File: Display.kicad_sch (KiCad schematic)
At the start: 2 parts

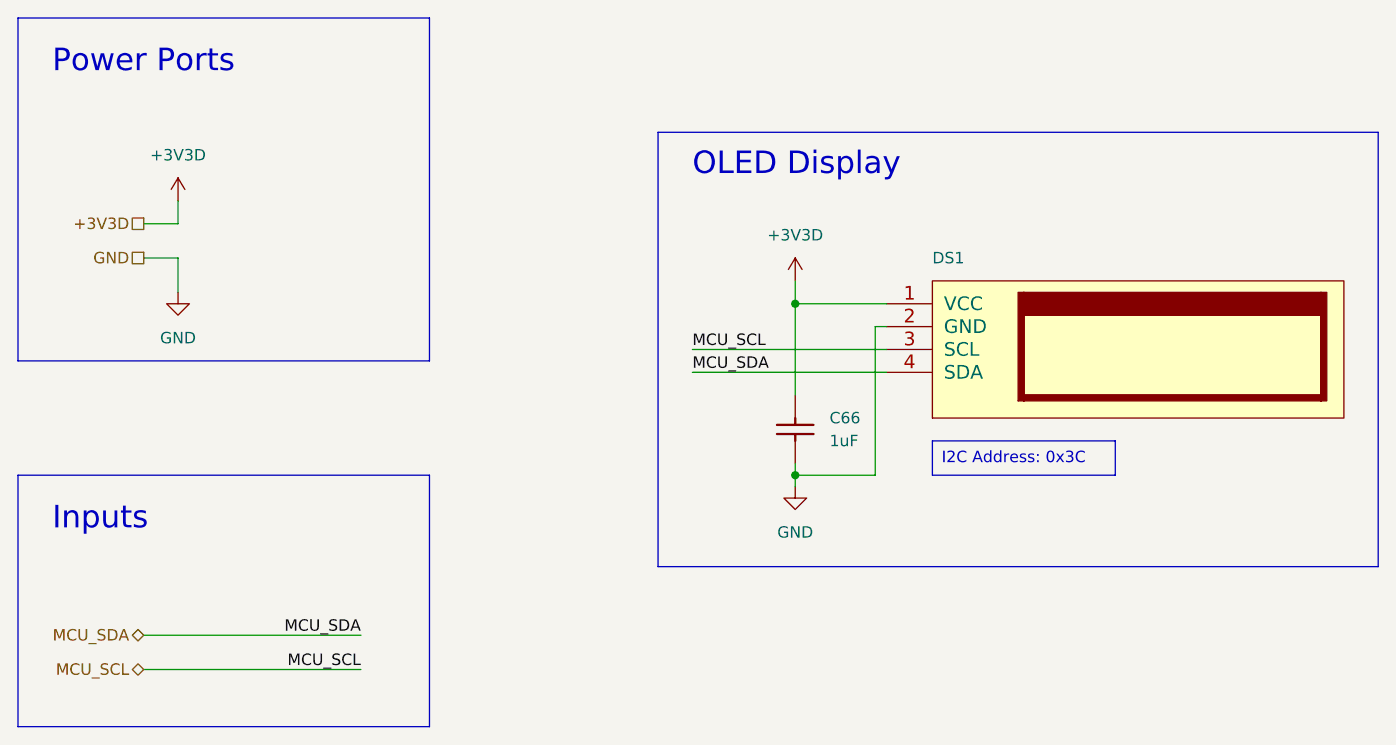
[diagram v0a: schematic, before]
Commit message: Reannotated schematic, added PSU calculation, some polish
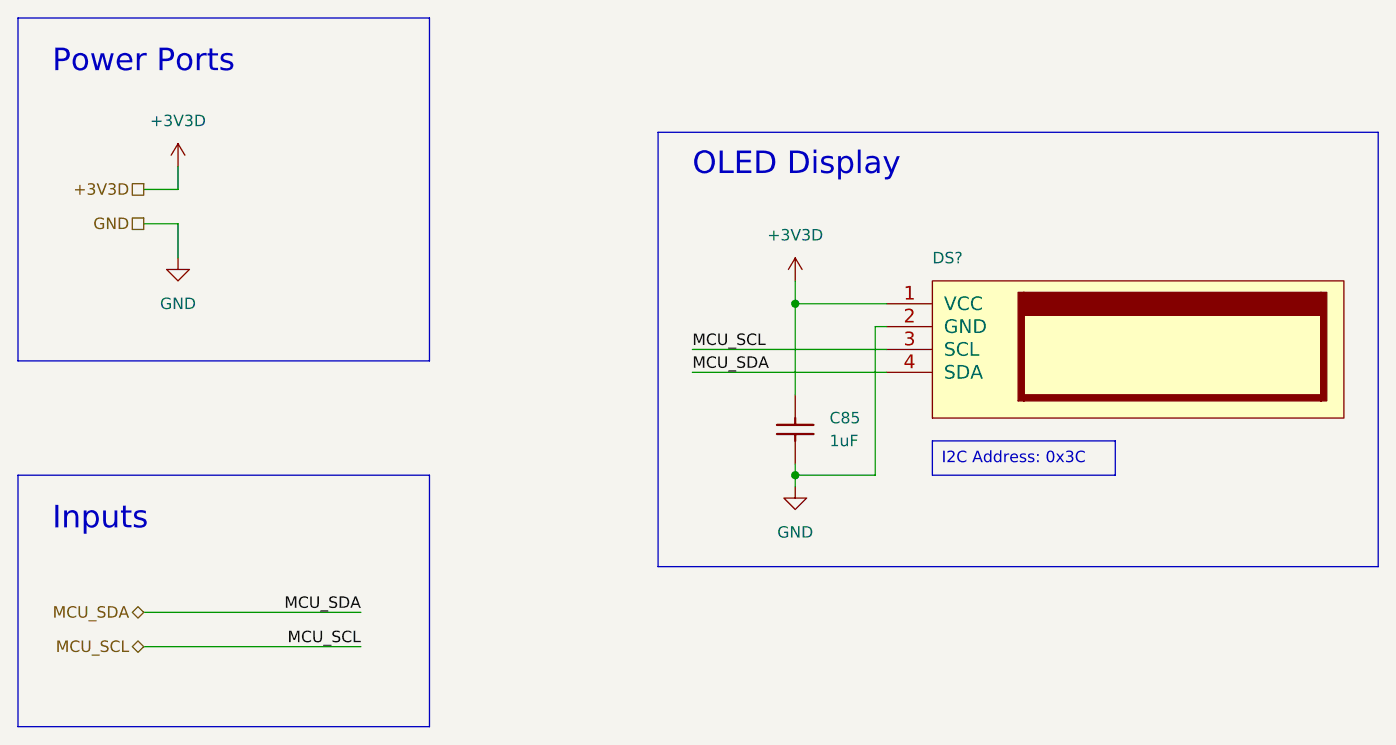
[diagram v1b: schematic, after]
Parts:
- renumbered C66 to C85, DS1 to DS?

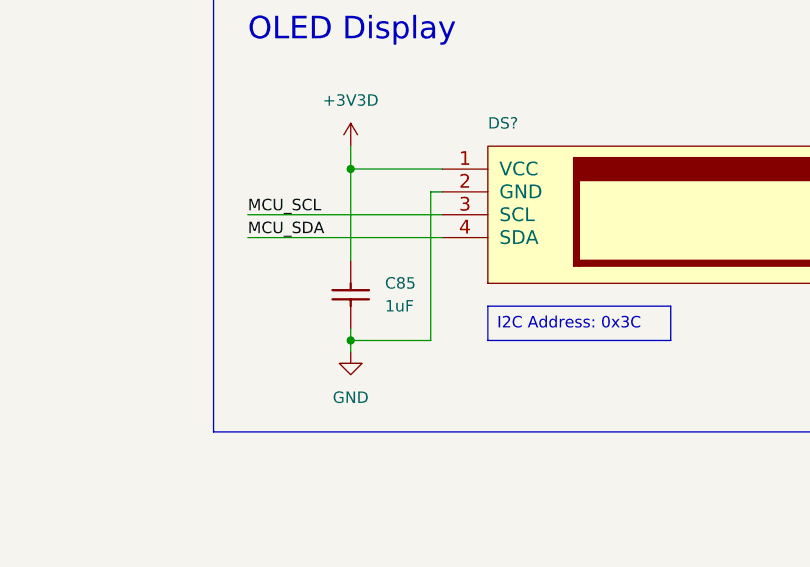
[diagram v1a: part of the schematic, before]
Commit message: Added OTA ADC
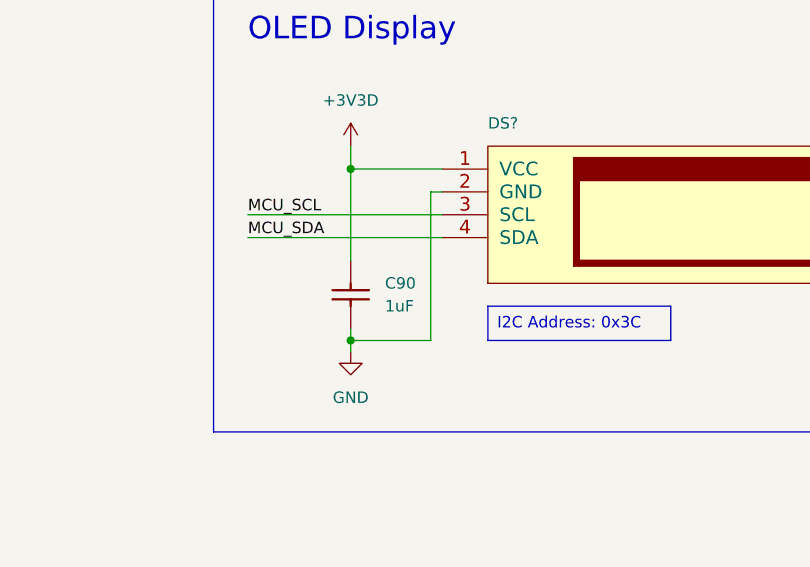
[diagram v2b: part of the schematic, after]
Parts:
- renumbered C85 to C90
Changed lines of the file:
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@@
         )
         (path "/d3b6a045-fd77-42ad-b330-1b1925488537/59667e70-bb75-464b-9655-2a4f5dbb3db0"
-          (reference "#PWR0313") (unit 1)
+          (reference "#PWR0219") (unit 1)
         )
       )
@@
   (symbol (lib_id "symbol_lib:+3V3D") (at 109.22 48.26 0) (unit 1)
     (in_bom yes) (on_board yes) (dnp no) (fields_autoplaced)
-    (property "Reference" "#PWR0312" (at 109.22 52.07 0)
+    (property "Reference" "#PWR0221" (at 109.22 52.07 0)
       (effects (font (size 1.27 1.27)) hide)
     )
@@
       (project "Accurate_Eval"
         (path "/d3b6a045-fd77-42ad-b330-1b1925488537/59667e70-bb75-464b-9655-2a4f5dbb3db0"
-          (reference "#PWR0312") (unit 1)
+          (reference "#PWR0221") (unit 1)
         )
       )
@@
   (symbol (lib_id "power:GND") (at 109.22 71.12 0) (unit 1)
     (in_bom yes) (on_board yes) (dnp no) (fields_autoplaced)
-    (property "Reference" "#PWR0311" (at 109.22 77.47 0)
+    (property "Reference" "#PWR0222" (at 109.22 77.47 0)
       (effects (font (size 1.27 1.27)) hide)
     )
@@
       (project "Accurate_Eval"
         (path "/d3b6a045-fd77-42ad-b330-1b1925488537/59667e70-bb75-464b-9655-2a4f5dbb3db0"
-          (reference "#PWR0311") (unit 1)
+          (reference "#PWR0222") (unit 1)
         )
       )
@@
   (symbol (lib_id "Capacitors SMD:CC0603_1UF_16V_10%_X7R") (at 109.22 60.96 270) (unit 1)
     (in_bom yes) (on_board yes) (dnp no) (fields_autoplaced)
-    (property "Reference" "C85" (at 113.03 63.5 90)
+    (property "Reference" "C90" (at 113.03 63.5 90)
       (effects (font (size 1.27 1.27)) (justify left))
     )
@@
       (project "Accurate_Eval"
         (path "/d3b6a045-fd77-42ad-b330-1b1925488537/59667e70-bb75-464b-9655-2a4f5dbb3db0"
-          (reference "C85") (unit 1)
+          (reference "C90") (unit 1)
         )
       )
@@
         )
         (path "/d3b6a045-fd77-42ad-b330-1b1925488537/59667e70-bb75-464b-9655-2a4f5dbb3db0"
-          (reference "#PWR0314") (unit 1)
-        )
-      )
+          (reference "#PWR0220") (unit 1)
+        )
+      )

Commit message: Fixed comments after schematics review from Clyde
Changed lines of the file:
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@@
     (effects (font (size 2.5 2.5)) (justify left bottom))
   )
-  (text "OLED Display" (at 97.79 36.83 0)
+  (text "OLED Display" (at 97.79 38.1 0)
     (effects (font (size 2.5 2.5)) (justify left bottom))
   )

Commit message: Fixed some visual details
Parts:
- renumbered C90 to C89
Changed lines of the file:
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@@
   (symbol (lib_id "Capacitors SMD:CC0603_1UF_16V_10%_X7R") (at 109.22 60.96 270) (unit 1)
     (in_bom yes) (on_board yes) (dnp no) (fields_autoplaced)
-    (property "Reference" "C90" (at 113.03 63.5 90)
+    (property "Reference" "C89" (at 113.03 63.5 90)
       (effects (font (size 1.27 1.27)) (justify left))
     )
@@
       (project "Accurate_Eval"
         (path "/d3b6a045-fd77-42ad-b330-1b1925488537/59667e70-bb75-464b-9655-2a4f5dbb3db0"
-          (reference "C90") (unit 1)
+          (reference "C89") (unit 1)
         )
       )

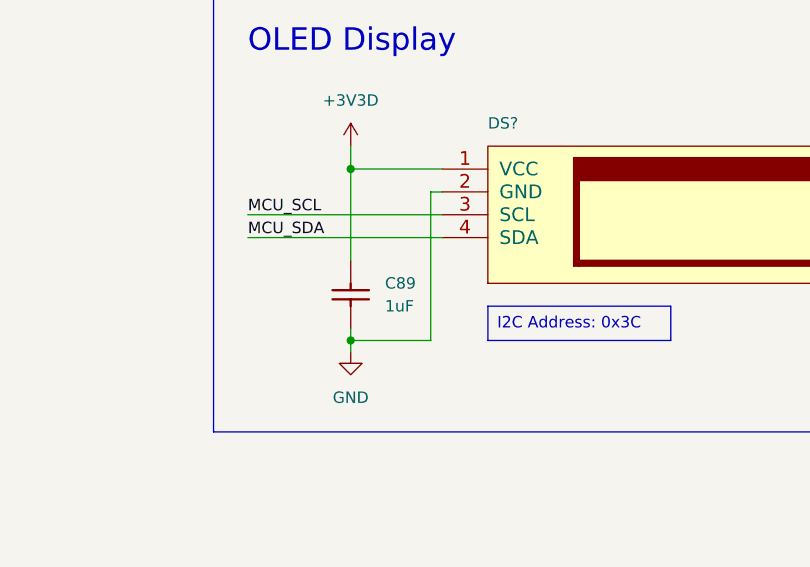
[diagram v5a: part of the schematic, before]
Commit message: Replaced buffers, added both bonded and packaged ACCURATE
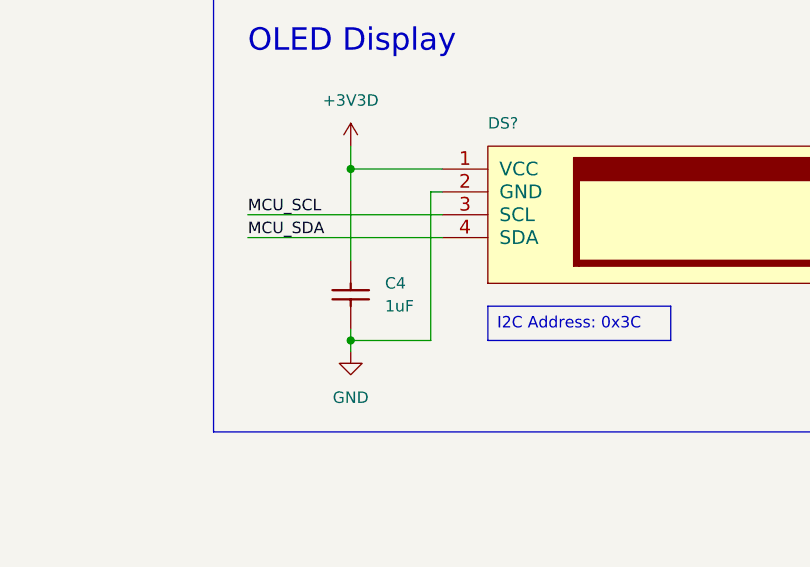
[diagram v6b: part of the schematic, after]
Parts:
- removed C89: CC0603_1UF_16V_10%_X7R, Capacitors SMD:CAPC1608X87N, symbol Capacitors SMD:CC0603_1UF_16V_10%_X7R
- added C4: CC0603_1UF_25V_10%_X7R, Capacitors SMD:CAPC1608X87N, symbol Capacitors SMD:CC0603_1UF_25V_10%_X7R
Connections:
- net +3V3D: now also C4.1
- net GND: now also C4.2
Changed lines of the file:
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@@
     )
   )
-  (symbol (lib_id "power:GND") (at 109.22 71.12 0) (unit 1)
-    (in_bom yes) (on_board yes) (dnp no) (fields_autoplaced)
-    (property "Reference" "#PWR0216" (at 109.22 77.47 0)
-      (effects (font (size 1.27 1.27)) hide)
-    )
-    (property "Value" "GND" (at 109.22 76.2 0)
-      (effects (font (size 1.27 1.27)))
-    )
-    (property "Footprint" "" (at 109.22 71.12 0)
-      (effects (font (size 1.27 1.27)) hide)
-    )
-    (property "Datasheet" "" (at 109.22 71.12 0)
-      (effects (font (size 1.27 1.27)) hide)
-    )
-    (pin "1")
-    (instances
-      (project "Accurate_Eval"
-        (path "/d3b6a045-fd77-42ad-b330-1b1925488537/59667e70-bb75-464b-9655-2a4f5dbb3db0"
-          (reference "#PWR0216") (unit 1)
-        )
-      )
-    )
-  )
-  (symbol (lib_id "Capacitors SMD:CC0603_1UF_16V_10%_X7R") (at 109.22 60.96 270) (unit 1)
-    (in_bom yes) (on_board yes) (dnp no) (fields_autoplaced)
-    (property "Reference" "C89" (at 113.03 63.5 90)
+  (symbol (lib_id "Capacitors SMD:CC0603_1UF_25V_10%_X7R") (at 109.22 60.96 270) (unit 1)
+    (in_bom yes) (on_board yes) (dnp no)
+    (property "Reference" "C4" (at 113.03 63.5 90)
       (effects (font (size 1.27 1.27)) (justify left))
     )
-    (property "Value" "CC0603_1UF_16V_10%_X7R" (at 102.997 60.96 0)
+    (property "Value" "CC0603_1UF_25V_10%_X7R" (at 102.997 60.96 0)
       (effects (font (size 1.27 1.27)) (justify left) hide)
     )
@@
       (effects (font (size 1.27 1.27)) (justify left) hide)
     )
-    (property "Datasheet" "\\\\cern.ch\\dfs\\Applications\\Altium\\Datasheets\\CC0603_X7R_PHYCOMP.pdf" (at 99.187 60.96 0)
+    (property "Datasheet" "\\\\cern.ch\\dfs\\Applications\\Altium\\Datasheets\\CC0603_X7R_MURATA.pdf" (at 99.187 60.96 0)
       (effects (font (size 1.27 1.27)) (justify left) hide)
     )
@@
       (effects (font (size 1.27 1.27)) (justify left))
     )
-    (property "Part Number" "CC0603_1UF_16V_10%_X7R" (at 97.282 60.96 0)
+    (property "Part Number" "CC0603_1UF_25V_10%_X7R" (at 97.282 60.96 0)
       (effects (font (size 1.27 1.27)) (justify left) hide)
     )
@@
       (effects (font (size 1.27 1.27)) (justify left) hide)
     )
-    (property "Voltage" "16V" (at 74.422 60.96 0)
+    (property "Voltage" "25V" (at 74.422 60.96 0)
       (effects (font (size 1.27 1.27)) (justify left) hide)
     )
@@
       (effects (font (size 1.27 1.27)) (justify left) hide)
     )
-    (property "Manufacturer Part Number" "CC0603_1UF_16V_10%_X7R" (at 64.897 60.96 0)
+    (property "Manufacturer Part Number" "CC0603_1UF_25V_10%_X7R" (at 64.897 60.96 0)
       (effects (font (size 1.27 1.27)) (justify left) hide)
     )
@@
       (effects (font (size 1.27 1.27)) (justify left) hide)
     )
-    (property "Manufacturer1 Example" "YAGEO PHYCOMP" (at 47.752 60.96 0)
+    (property "Manufacturer1 Example" "MURATA" (at 47.752 60.96 0)
       (effects (font (size 1.27 1.27)) (justify left) hide)
     )
-    (property "Manufacturer1 Part Number" "223878615663" (at 45.847 60.96 0)
+    (property "Manufacturer1 Part Number" "GRM188R71E105KA12D" (at 45.847 60.96 0)
       (effects (font (size 1.27 1.27)) (justify left) hide)
     )
@@
       (effects (font (size 1.27 1.27)) (justify left) hide)
     )
-    (property "HelpURL" "\\\\cern.ch\\dfs\\Applications\\Altium\\Datasheets\\CC0603_X7R_PHYCOMP.pdf" (at 42.037 60.96 0)
+    (property "HelpURL" "\\\\cern.ch\\dfs\\Applications\\Altium\\Datasheets\\CC0603_X7R_MURATA.pdf" (at 42.037 60.96 0)
       (effects (font (size 1.27 1.27)) (justify left) hide)
     )
@@
       (effects (font (size 1.27 1.27)) (justify left) hide)
     )
-    (property "CreateDate" "12/03/07 00:00:00" (at 38.227 60.96 0)
+    (property "CreateDate" "01/18/11 00:00:00" (at 38.227 60.96 0)
       (effects (font (size 1.27 1.27)) (justify left) hide)
     )
-    (property "LatestRevisionDate" "04/17/15 00:00:00" (at 36.322 60.96 0)
+    (property "LatestRevisionDate" "01/18/11 00:00:00" (at 36.322 60.96 0)
       (effects (font (size 1.27 1.27)) (justify left) hide)
     )
@@
     (instances
       (project "Accurate_Eval"
+        (path "/d3b6a045-fd77-42ad-b330-1b1925488537/3601916a-1298-4c62-aaea-496828b211de"
+          (reference "C4") (unit 1)
+        )
         (path "/d3b6a045-fd77-42ad-b330-1b1925488537/59667e70-bb75-464b-9655-2a4f5dbb3db0"
           (reference "C89") (unit 1)
         )
       )
+    )
+  )
+  (symbol (lib_id "power:GND") (at 109.22 71.12 0) (unit 1)
+    (in_bom yes) (on_board yes) (dnp no) (fields_autoplaced)
+    (property "Reference" "#PWR0216" (at 109.22 77.47 0)
+      (effects (font (size 1.27 1.27)) hide)
+    )
+    (property "Value" "GND" (at 109.22 76.2 0)
+      (effects (font (size 1.27 1.27)))
+    )
+    (property "Footprint" "" (at 109.22 71.12 0)
+      (effects (font (size 1.27 1.27)) hide)
+    )
+    (property "Datasheet" "" (at 109.22 71.12 0)
+      (effects (font (size 1.27 1.27)) hide)
+    )
+    (pin "1")
+    (instances
+      (project "Accurate_Eval"
+        (path "/d3b6a045-fd77-42ad-b330-1b1925488537/59667e70-bb75-464b-9655-2a4f5dbb3db0"
+          (reference "#PWR0216") (unit 1)
+        )
+      )

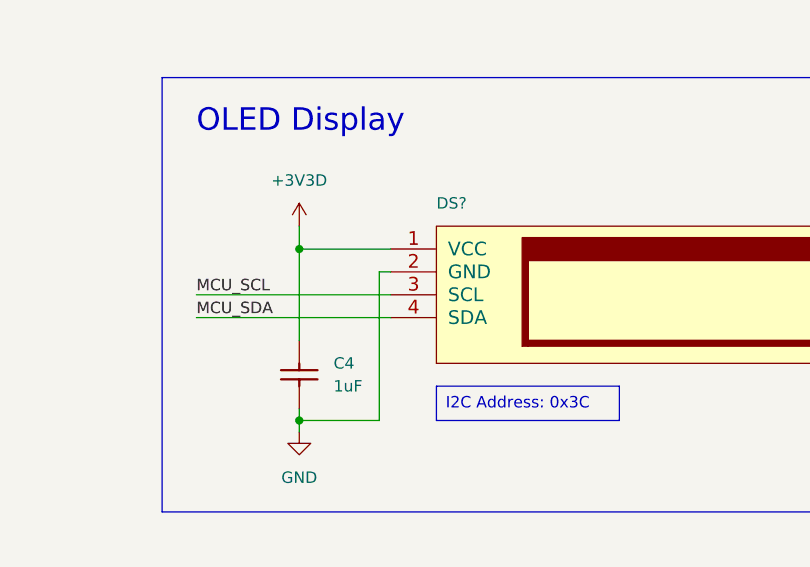
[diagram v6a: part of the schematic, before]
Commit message: Updated schematic after routing, added layout
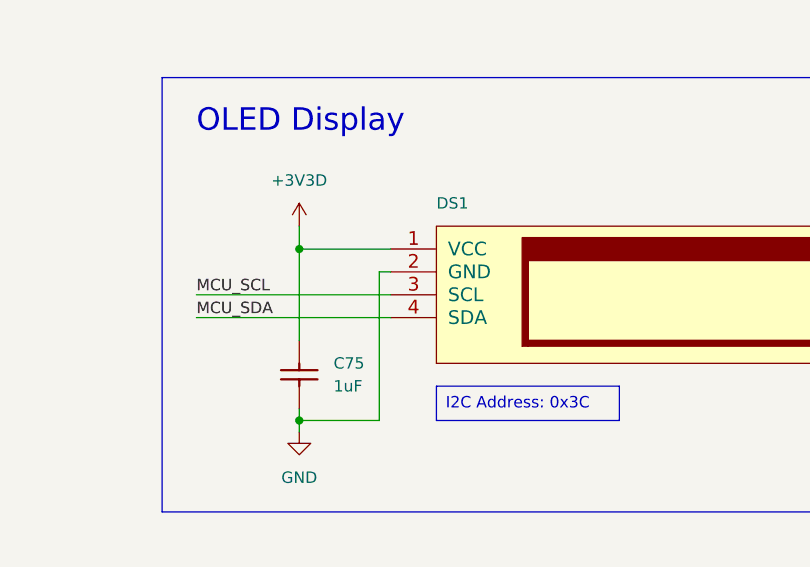
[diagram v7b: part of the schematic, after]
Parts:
- gave numbers to parts that had none: 1
- renumbered C4 to C75

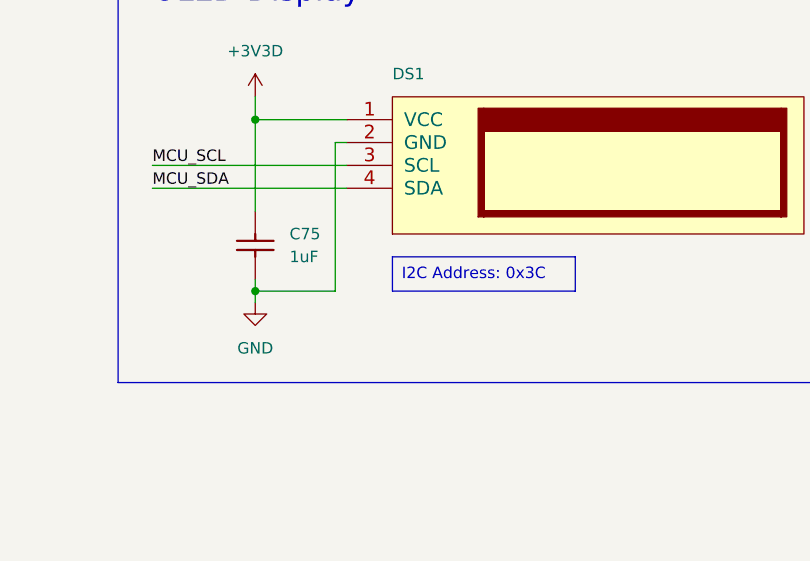
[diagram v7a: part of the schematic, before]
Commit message: Annotation now matches the produced PCB
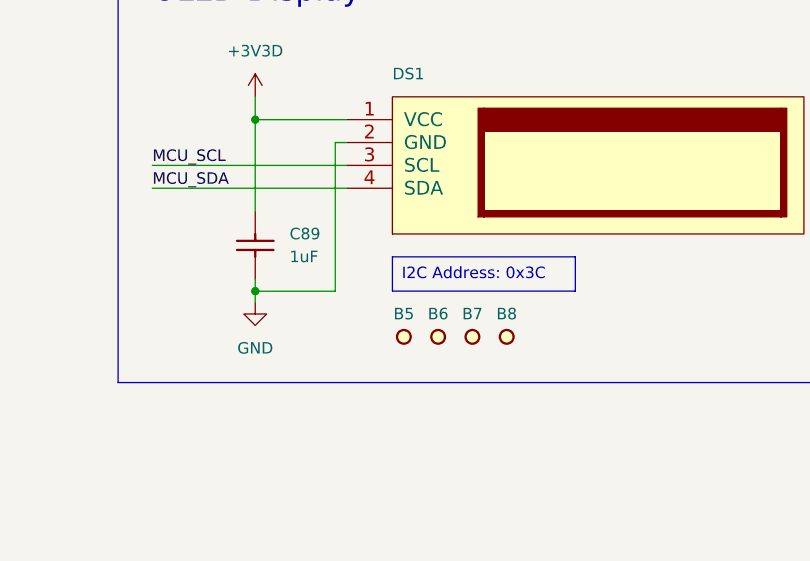
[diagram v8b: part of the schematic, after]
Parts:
- added B5, B6, B7, B8: NON-PLATED_HOLE2.5, Pads:MTG250, symbol Pads:NON-PLATED_HOLE2.5
- renumbered C75 to C89
